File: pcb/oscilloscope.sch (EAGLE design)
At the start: 37 parts, among them J1 35PM1, J2 35PM1, J3 35PM1, J4 35PM1, J5 35PM1, J6 35PM1, J7 35PM1, J8 35PM1, M1 ESP32, SW1 EN12-HS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

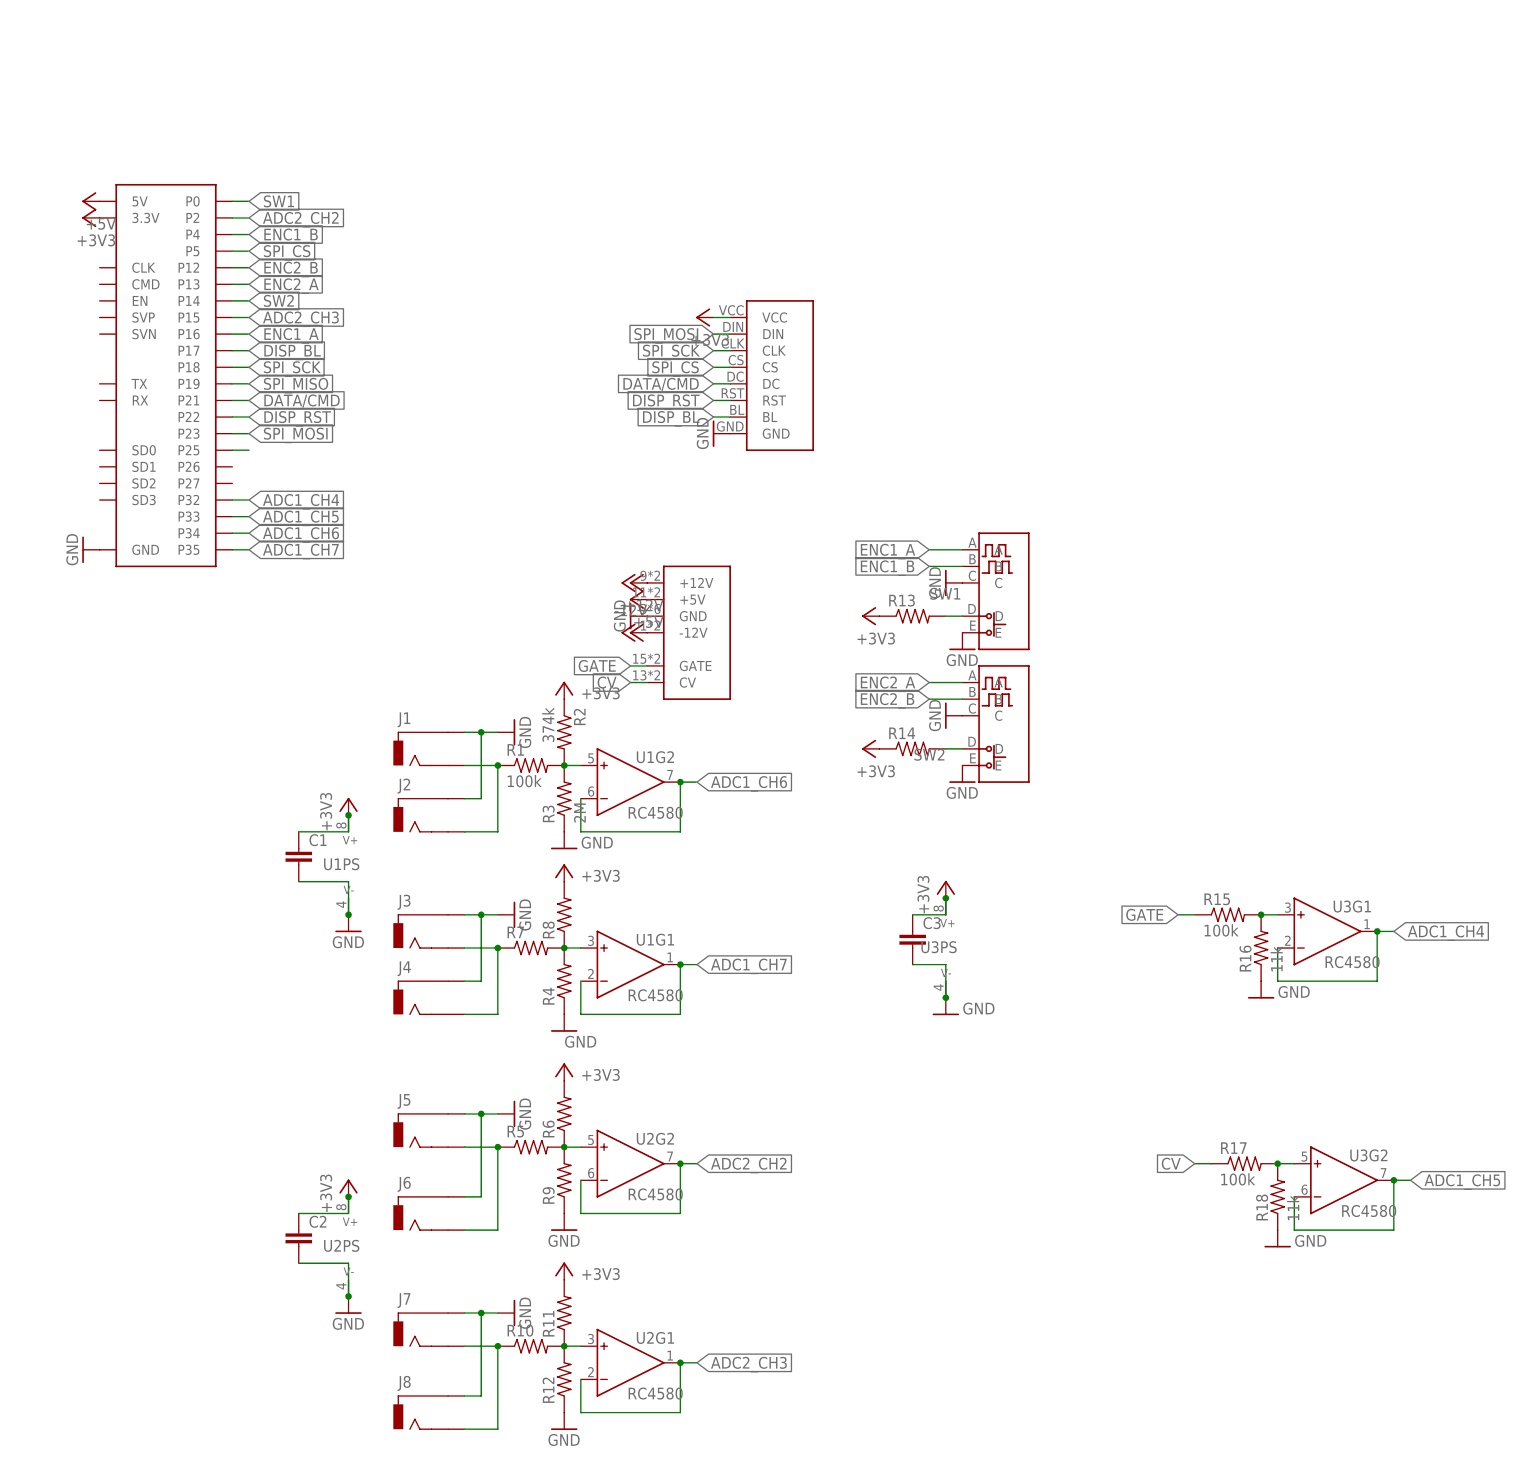
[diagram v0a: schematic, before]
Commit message: Updating PCB to rev B
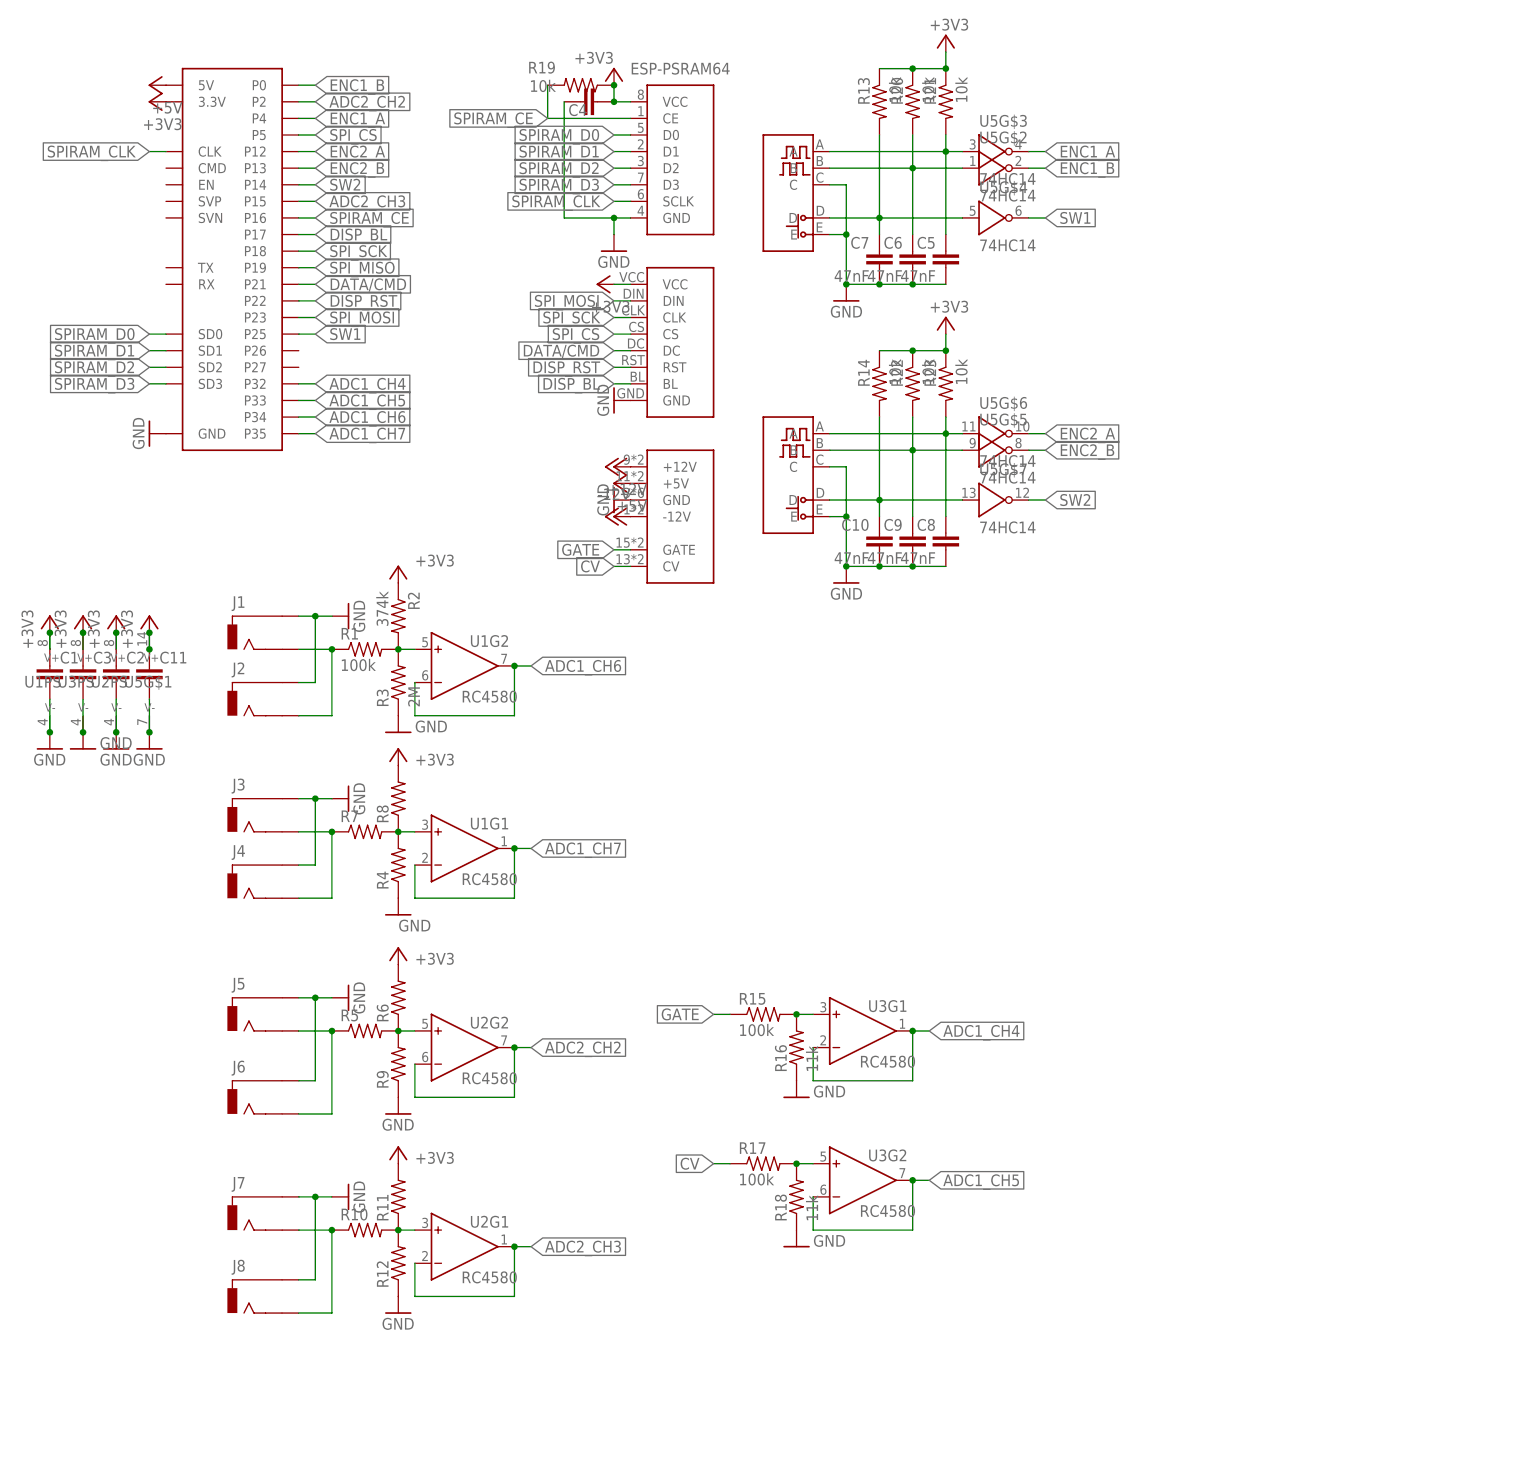
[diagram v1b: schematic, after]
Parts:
- added C10, C5, C6, C7, C8, C9: 47nF, rcl:C-EUC0805
- added C11, C4: (no value), rcl:C-EUC0805
- added R19, R20, R21, R22, R23: 10k, rcl:R-US_R0805
- added U4: ESP-PSRAM64, artysynth:ESP-PSRAM64
- added U5: 74HC14, artysynth:74HC14
- R13, R14: value (none) -> 10k
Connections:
- removed net ADC2_CH8: M1.P25
- new net ENC1_A_I: C5.1, R21.2, SW1.A, U5G$3.I
- new net ENC1_B_I: C6.1, R20.2, SW1.B, U5G$2.I
- new net ENC2_A_I: C8.1, R23.2, SW2.A, U5G$6.I
- new net ENC2_B_I: C9.1, R22.2, SW2.B, U5G$5.I
- new net SPIRAM_CE: M1.P16, R19.2, U4.CE
- new net SPIRAM_CLK: M1.CLK, U4.SCLK
- new net SPIRAM_D0: M1.SD0, U4.D0
- new net SPIRAM_D1: M1.SD1, U4.D1
- new net SPIRAM_D2: M1.SD2, U4.D2
- new net SPIRAM_D3: M1.SD3, U4.D3
- new net SW1_I: C7.1, R13.2, SW1.D, U5G$4.I
- new net SW2_I: C10.1, R14.2, SW2.D, U5G$7.I
- net +3V3: now also C11.1, C4.2, R19.1, R20.1, R21.1, R22.1, R23.1, U4.VCC, U5G$1.V+
- net ENC1_A: now also M1.P4, U5G$3.O; no longer M1.P16, SW1.A
- net ENC1_B: now also M1.P0, U5G$2.O; no longer M1.P4, SW1.B
- net ENC2_A: now also M1.P12, U5G$6.O; no longer M1.P13, SW2.A
- net ENC2_B: now also M1.P13, U5G$5.O; no longer M1.P12, SW2.B
- net GND: now also C10.2, C11.2, C4.1, C5.2, C6.2, C7.2, C8.2, C9.2, U4.GND, U5G$1.V-
- net SW1: now also M1.P25, U5G$4.O; no longer M1.P0, R13.2, SW1.D
- net SW2: now also U5G$7.O; no longer R14.2, SW2.D
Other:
- moved on the sheet: C1, C2, C3, J1, J2, J3, J4, J5, J6, J7, J8, R1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
